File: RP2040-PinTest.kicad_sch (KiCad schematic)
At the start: 3 parts

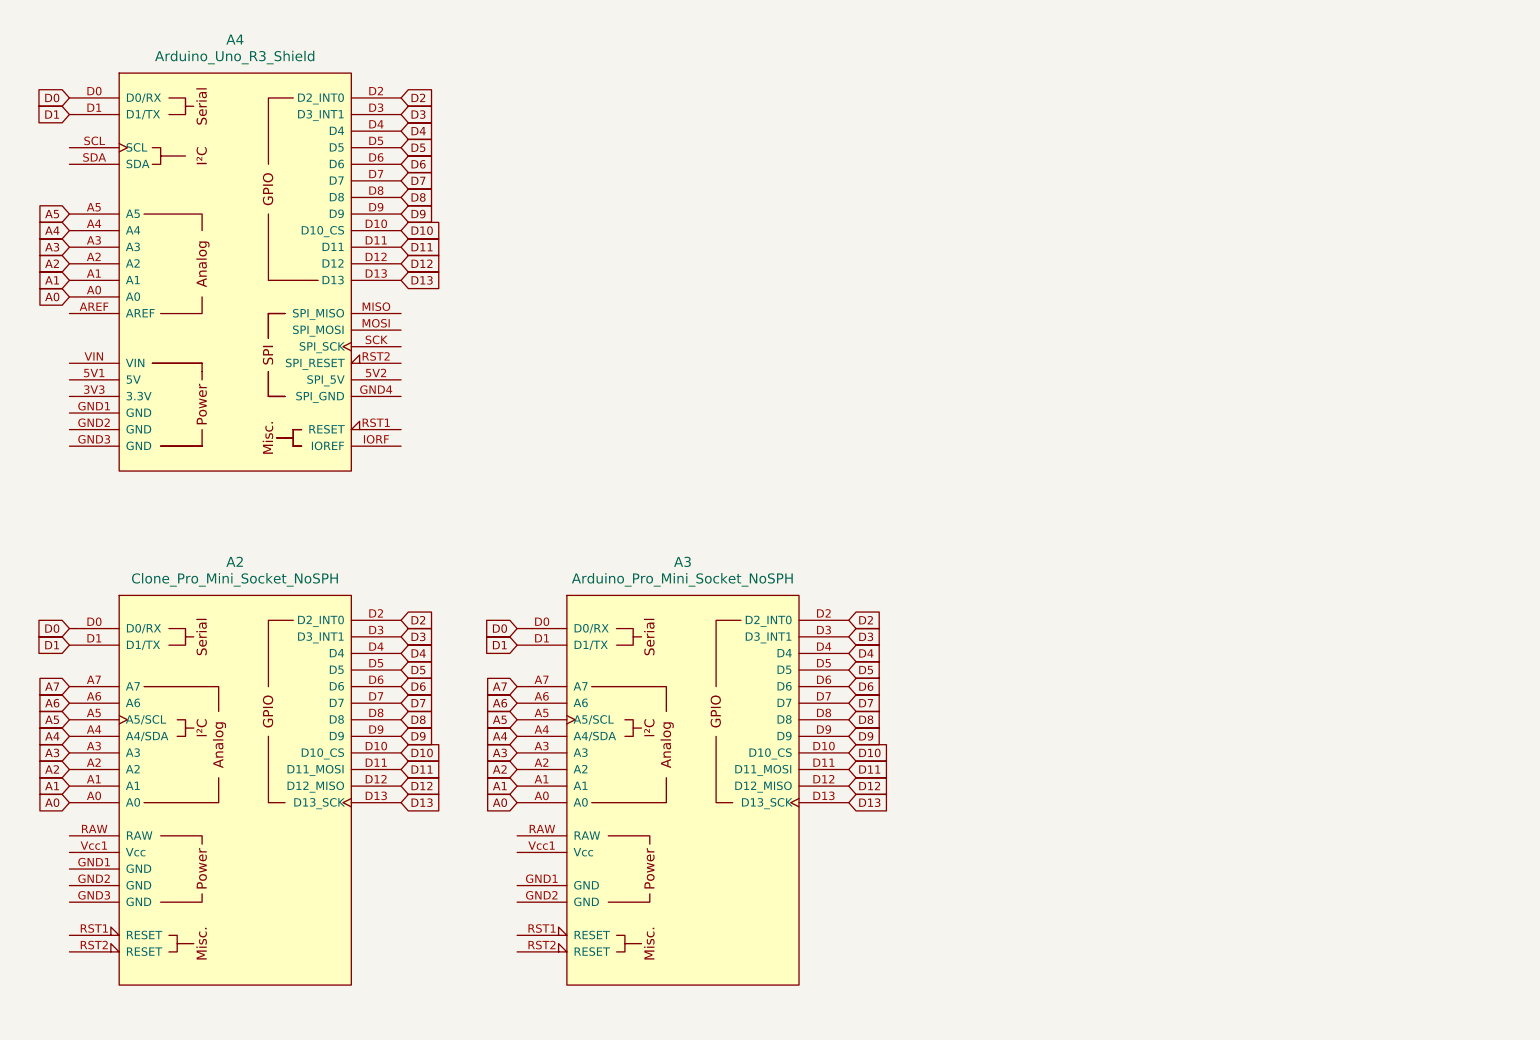
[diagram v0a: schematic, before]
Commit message: Added more pins
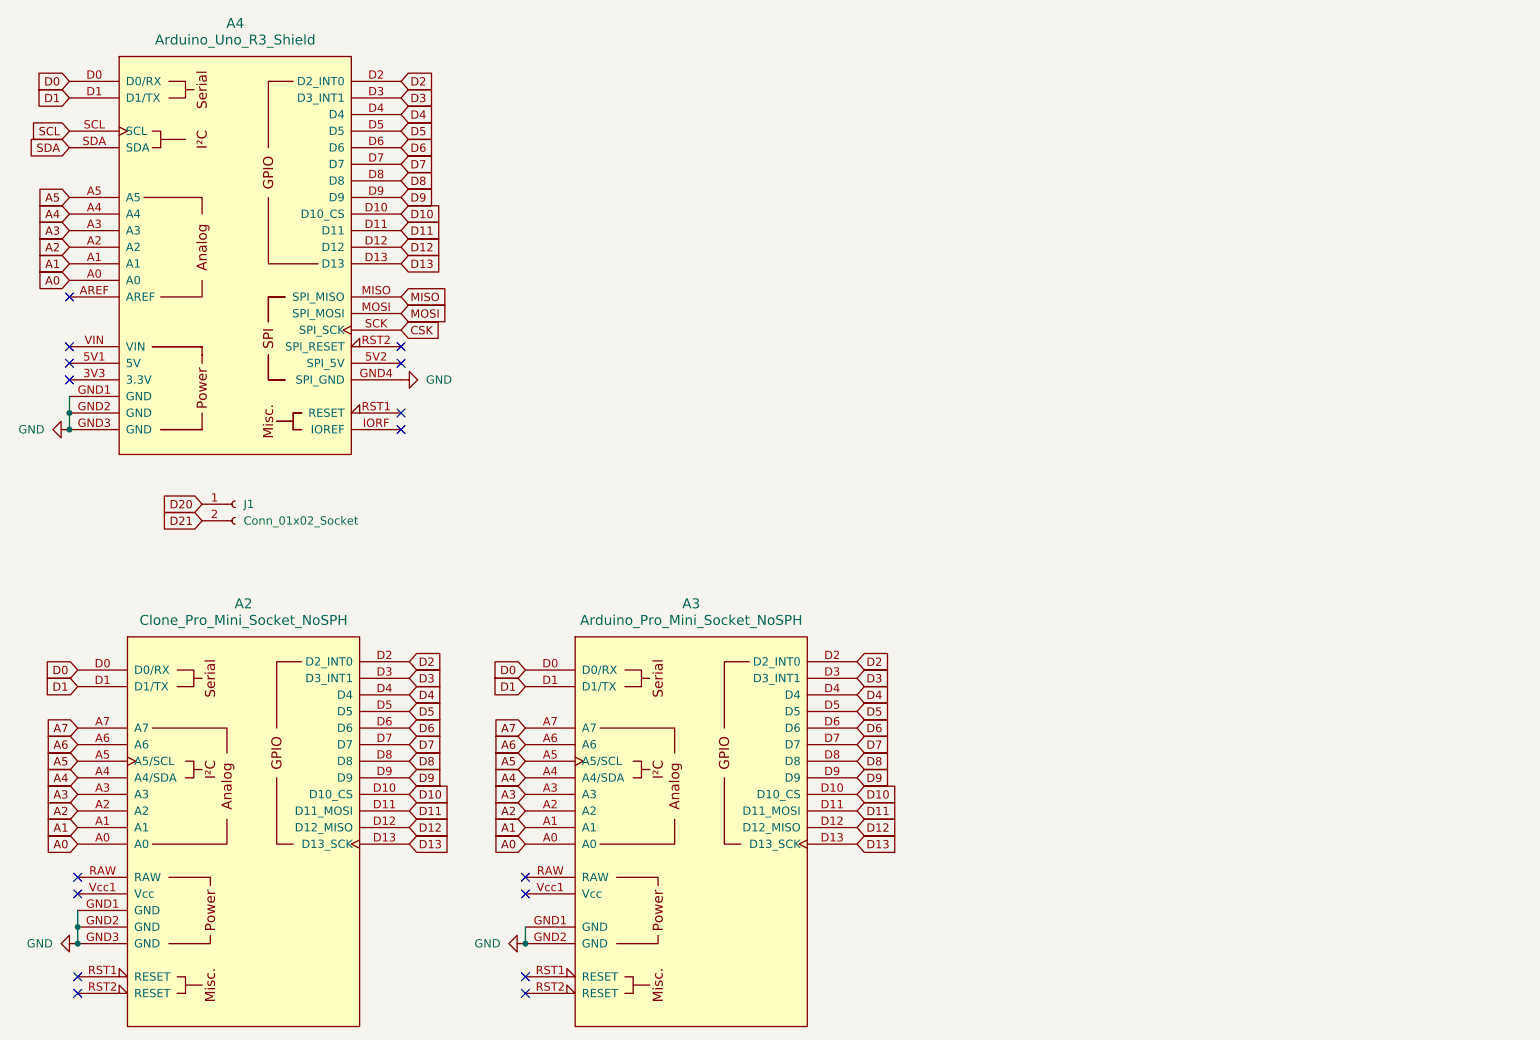
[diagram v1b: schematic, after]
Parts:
- added J1: Conn_01x02_Socket, Connector_PinSocket_2.54mm:PinSocket_1x02_P2.54mm_Vertical, symbol Connector:Conn_01x02_Socket
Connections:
- net GND: now reaches A4.GND1 (GND)
- net GND: now also A2.GND1 (GND), A2.GND2 (GND), A2.GND3 (GND), A3.GND1 (GND), A3.GND2 (GND), A4.GND2 (GND), A4.GND3 (GND), A4.GND4 (SPI_GND)
- net MISO: now reaches A4.MISO (SPI_MISO)
- net MOSI: now reaches A4.MOSI (SPI_MOSI)
- net CSK: now reaches A4.SCK (SPI_SCK)
- net SCL: now reaches A4.SCL
- net SDA: now reaches A4.SDA
- new net D20: J1.1 (Pin_1)
- new net D21: J1.2 (Pin_2)
- no-connect marks 0 -> 16
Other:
- moved on the sheet: A2, A3, A4

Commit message: Added LEDs and basic routing
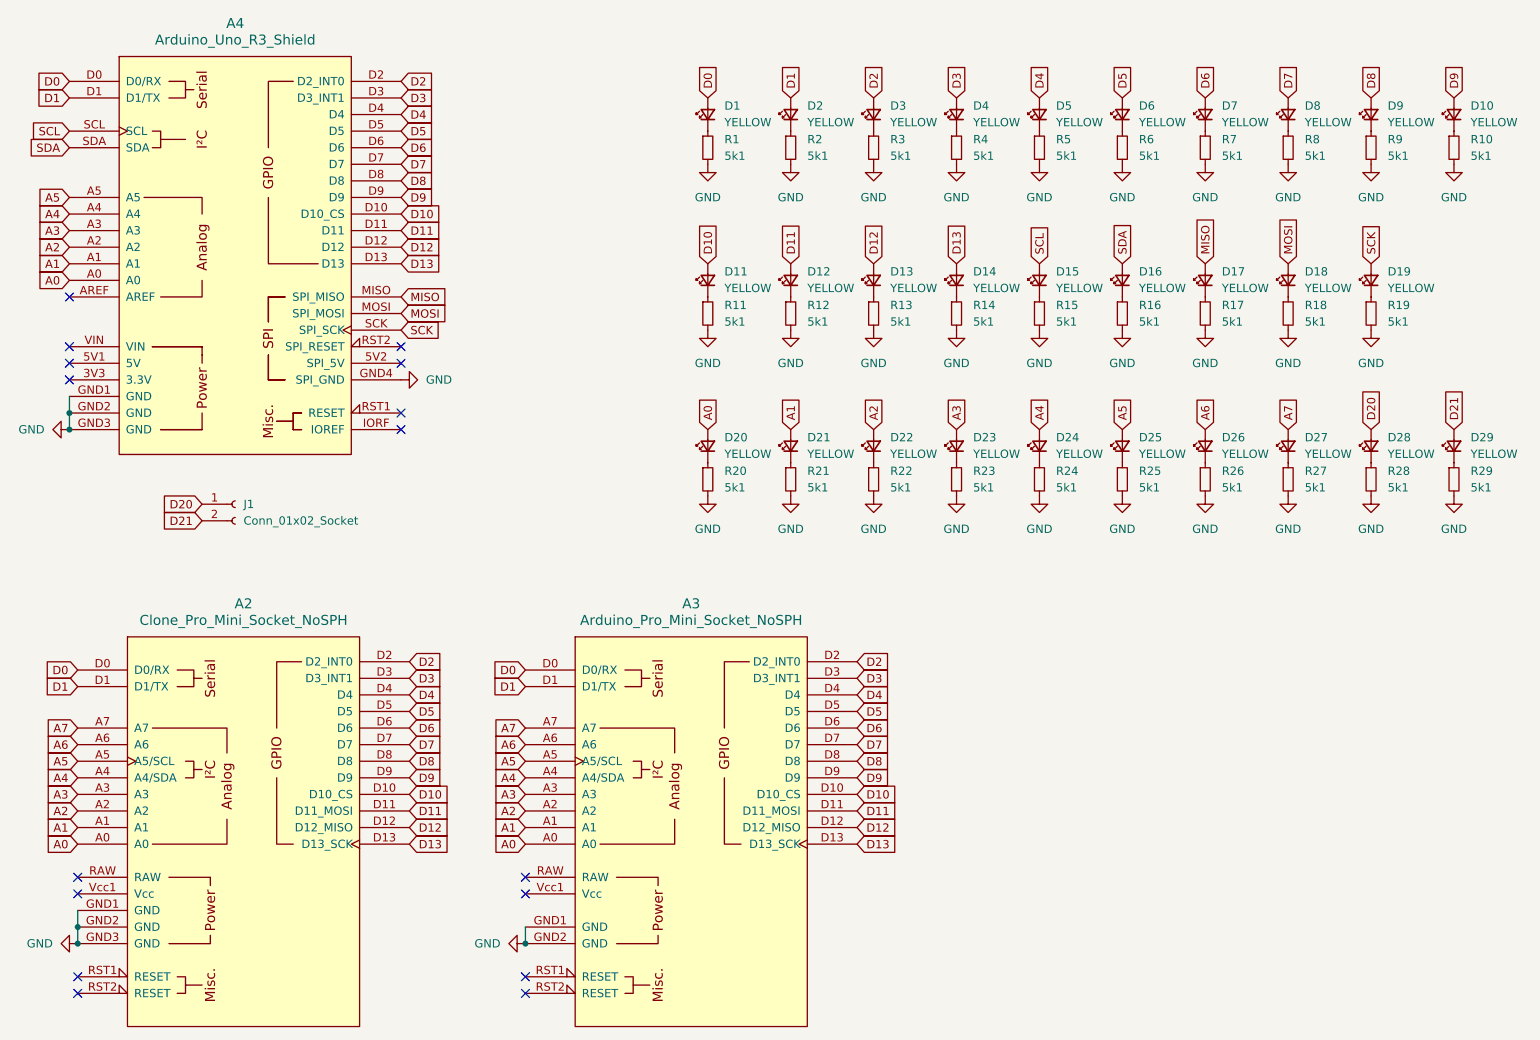
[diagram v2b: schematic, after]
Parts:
- added D1, D10, D11, D12, D13, D14, D15, D16, D17, D18, D19, D2, D20, D21, D22, D23, D24, D25, D26, D27, D28, D29, D3, D4, D5, D6, D7, D8, D9: YELLOW, LED_SMD:LED_0603_1608Metric, symbol Device:LED_Small
- added R1, R10, R11, R12, R13, R14, R15, R16, R17, R18, R19, R2, R20, R21, R22, R23, R24, R25, R26, R27, R28, R29, R3, R4, R5, R6, R7, R8, R9: 5k1, Resistor_SMD:R_0603_1608Metric, symbol Device:R_Small
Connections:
- net A0: now also D20.2 (A)
- net A1: now also D21.2 (A)
- net A2: now also D22.2 (A)
- net A3: now also D23.2 (A)
- net A4: now also D24.2 (A)
- net A5: now also D25.2 (A)
- net A6: now also D26.2 (A)
- net A7: now also D27.2 (A)
- net D0: now also D1.2 (A)
- net D1: now also D2.2 (A)
- net D10: now also D11.2 (A)
- net D11: now also D12.2 (A)
- net D12: now also D13.2 (A)
- net D13: now also D14.2 (A)
- net D2: now also D3.2 (A)
- net D20: now also D28.2 (A)
- net D21: now also D29.2 (A)
- net D3: now also D4.2 (A)
- net D4: now also D5.2 (A)
- net D5: now also D6.2 (A)
- net D6: now also D7.2 (A)
- net D7: now also D8.2 (A)
- net D8: now also D9.2 (A)
- net D9: now also D10.2 (A)
- net GND: now also R1.2, R10.2, R11.2, R12.2, R13.2, R14.2, R15.2, R16.2, R17.2, R18.2, R19.2, R2.2, R20.2, R21.2, R22.2, R23.2, R24.2, R25.2, R26.2, R27.2, R28.2, R29.2, R3.2, R4.2, R5.2, R6.2, R7.2, R8.2, R9.2
- net MISO: now also D17.2 (A)
- net MOSI: now also D18.2 (A)
- net SCL: now also D15.2 (A)
- net SDA: now also D16.2 (A)
- net CSK renamed SCK
- net SCK: now also D19.2 (A)
- new net: D12.1 (K), R12.1
- new net: D28.1 (K), R28.1
- new net: D10.1 (K), R10.1
- new net: D15.1 (K), R15.1
- new net: D6.1 (K), R6.1
- new net: D4.1 (K), R4.1
- new net: D13.1 (K), R13.1
- new net: D20.1 (K), R20.1
- new net: D1.1 (K), R1.1
- new net: D2.1 (K), R2.1
- new net: D22.1 (K), R22.1
- new net: D29.1 (K), R29.1
- new net: D21.1 (K), R21.1
- new net: D14.1 (K), R14.1
- new net: D9.1 (K), R9.1
- new net: D23.1 (K), R23.1
- new net: D27.1 (K), R27.1
- new net: D3.1 (K), R3.1
- new net: D25.1 (K), R25.1
- new net: D26.1 (K), R26.1
- new net: D24.1 (K), R24.1
- new net: D7.1 (K), R7.1
- new net: D11.1 (K), R11.1
- new net: D17.1 (K), R17.1
- new net: D5.1 (K), R5.1
- new net: D8.1 (K), R8.1
- new net: D16.1 (K), R16.1
- new net: D18.1 (K), R18.1
- new net: D19.1 (K), R19.1
